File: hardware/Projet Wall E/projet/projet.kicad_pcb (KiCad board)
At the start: 2 copper layers, 91 parts, among them J201 USB_C_Receptacle_USB2.0_16P, J202 Conn_01x02, J301 Conn_ST_STDC14, J302 Conn_01x03, J401 Conn_01x06, J402 Conn_01x06, J501 Conn_01x06, J502 Conn_01x06, J503 Conn_01x03, J504 Conn_01x06, Q201 2SK3019, Q202 MMDT5401, Q203 DMP3099L, U201 AP2112K-3.3, U202 BQ27220YZFR, U203 USBLC6-2SC6, U204 BQ25896RTW, U301 STM32G431RBTx, U401 DRV8833PWP, U501 SN74AHCT1G125DBVR, Y301 16MHz

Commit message: PCB : contour 80x40, trous de fixation M2.5, sérigraphie
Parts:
- added C313: 1u, Capacitor_SMD:C_0402_1005Metric, F.Cu at (103.9, 87.5)
- added H301: MountingHole_Pad, MountingHole:MountingHole_2.2mm_M2_Pad_Via, F.Cu at (130.2, 116.8)
- added H302: MountingHole_Pad, MountingHole:MountingHole_2.2mm_M2_Pad_Via, F.Cu at (130.0, 123.5)
- added H303: MountingHole_Pad, MountingHole:MountingHole_2.2mm_M2_Pad_Via, F.Cu at (130.0, 129.4)
- added H304: MountingHole_Pad, MountingHole:MountingHole_2.2mm_M2_Pad_Via, F.Cu at (130.0, 135.4)
- C202: value 1µ -> 1u
- C301, C302, C303, C304: value 100nF -> 100n
- C305: value 4.7u -> 4u7
- C307, C312: value 1uF -> 1u
- moved C503 72.3 mm to (152.6, 106.0), turned to 90 degrees
- moved C509 70.7 mm to (153.0, 84.0)
- moved C502 70.3 mm to (150.6, 106.0), turned to 90 degrees
- moved C506 69.5 mm to (152.6, 103.1), turned to 90 degrees
- moved C505 67.4 mm to (150.6, 103.1), turned to 90 degrees
- moved C504 66.3 mm to (144.1, 76.5)
- moved C507 66.3 mm to (147.0, 76.5)
- moved C501 66.3 mm to (141.3, 76.5)
- moved C508 65.7 mm to (148.5, 84.0)
- moved R502 61.8 mm to (156.5, 95.5), turned to 90 degrees
- moved R501 59.6 mm to (154.5, 95.5), turned to 90 degrees
- moved J501 54.7 mm to (132.7, 105.1), turned to 90 degrees
- moved D501 49.1 mm to (134.0, 81.0), turned to 90 degrees
- moved J502 48.9 mm to (132.7, 100.5), turned to 90 degrees
- moved U501 42.9 mm to (136.1, 74.0)
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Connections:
- D501 pad 2: unconnected-(D501-DOUT-Pad2) -> Net-(D501-DOUT)
- J503 pad 2: /Capteur/NP_5V -> Net-(D501-DOUT)

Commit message: Ajout points de test + plans de masse PCB
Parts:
- added TP201: GND, TestPoint:TestPoint_Pad_D1.5mm, F.Cu at (104.1, 66.4)
- added TP202: VSYS, TestPoint:TestPoint_Pad_D1.0mm, F.Cu at (107.4, 66.1)
- added TP203: +3.3V, TestPoint:TestPoint_Pad_D1.0mm, F.Cu at (107.4, 69.2)
- added TP204: +5V_USB, TestPoint:TestPoint_Pad_D1.0mm, F.Cu at (110.4, 66.1)
- added TP205: VBUS, TestPoint:TestPoint_Pad_D1.0mm, F.Cu at (110.4, 69.2)
- added TP206: BAT, TestPoint:TestPoint_Pad_D1.0mm, F.Cu at (113.5, 66.1)
- added TP207: SCL, TestPoint:TestPoint_Pad_D1.0mm, F.Cu at (113.5, 69.2)
- added TP208: SDA, TestPoint:TestPoint_Pad_D1.0mm, F.Cu at (116.5, 66.1)
- added TP209: CHG_INT, TestPoint:TestPoint_Pad_D1.0mm, F.Cu at (116.5, 69.2)
- added TP210: GND, TestPoint:TestPoint_Pad_D1.5mm, F.Cu at (104.1, 69.9)
- added TP211: GND, TestPoint:TestPoint_Pad_D1.5mm, F.Cu at (104.1, 73.5)
- added TP401: MOT_nFAULT, TestPoint:TestPoint_Pad_D1.0mm, F.Cu at (108.9, 78.8)
- added TP501: SCL_CAPT, TestPoint:TestPoint_Pad_D1.0mm, F.Cu at (103.8, 78.8)
- added TP502: SDA_CAPT, TestPoint:TestPoint_Pad_D1.0mm, F.Cu at (103.8, 81.8)
- C201, C202, C203, C204, C205, C206, C207, C208, C209, C210, C211, C212, C401, C402, C403, D201, D202, F201, L201, Q201, Q202, Q203, R201, R202, R203, R204, R205, R206, R207, R208, R209, R210, R211, R212, R213, R214, R215, R216, R217, R218, R401, R402, R403, U201, U202, U203, U204, U401: moved to B.Cu
- moved R211 136.2 mm to (197.7, 82.3), turned to 180 degrees
- moved J201 135.9 mm to (200.2, 68.6), turned to 90 degrees
- moved R208 134.6 mm to (196.0, 76.8)
- moved R202 131.6 mm to (191.4, 63.9), turned to 180 degrees
- moved R203 131.6 mm to (191.4, 65.1), turned to 180 degrees
- moved R205 130.8 mm to (189.8, 78.9), turned to -90 degrees
- moved R207 130.2 mm to (190.9, 78.9), turned to 90 degrees
- moved Q203 127.6 mm to (200.2, 78.8), turned to 90 degrees
- moved J302 121.9 mm to (187.5, 87.0), turned to 90 degrees
- moved R206 119.6 mm to (178.0, 84.5), turned to 180 degrees
- moved Q202 119.1 mm to (196.4, 78.8)
- moved J202 118.9 mm to (191.2, 55.5), turned to 180 degrees
- moved C201 118.2 mm to (174.4, 63.6), turned to 135 degrees
- moved U203 118.1 mm to (190.8, 68.5), turned to 90 degrees
- moved R303 118.0 mm to (186.0, 81.2)
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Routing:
- net GND: track 0.00 -> 23.8 mm, vias 0 -> 73
- added copper zone on In1.Cu, net GND
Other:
- copper layers 2 -> 4

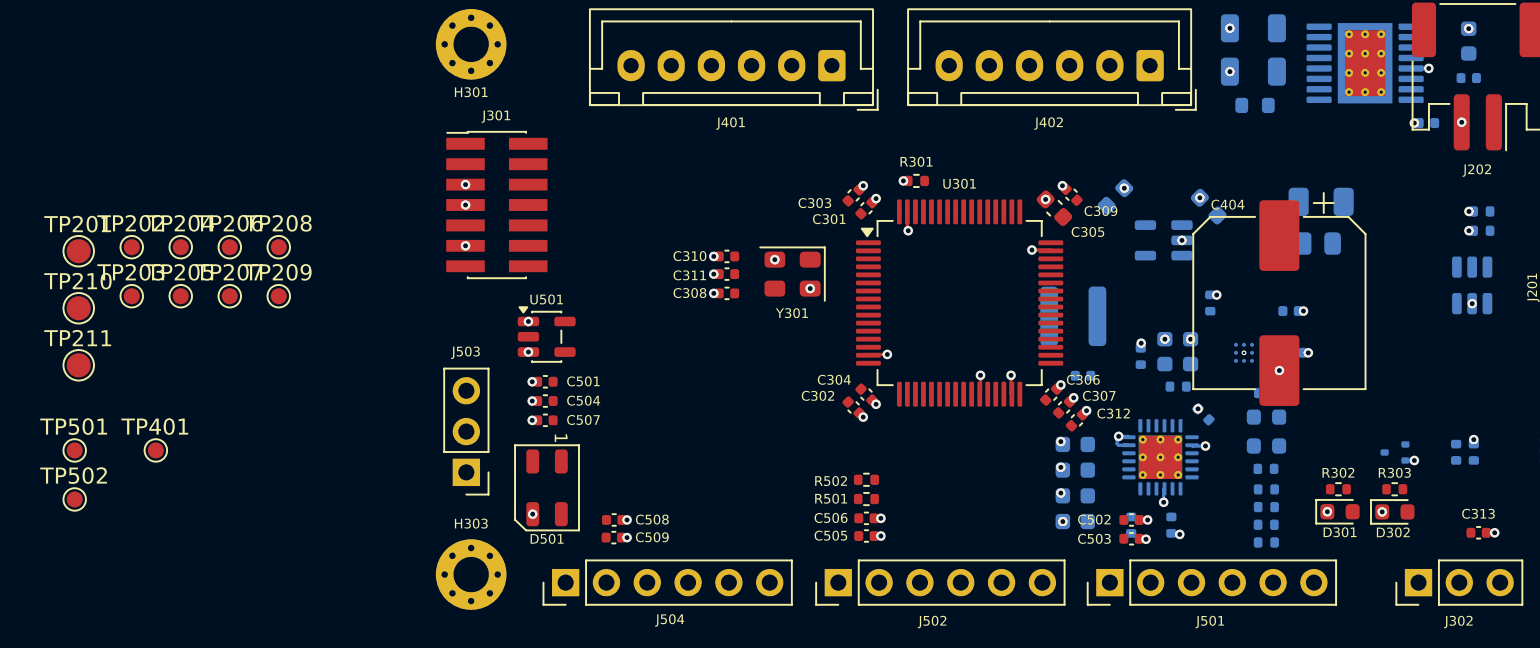
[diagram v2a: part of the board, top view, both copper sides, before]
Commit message: PCB : placement composants et points de test
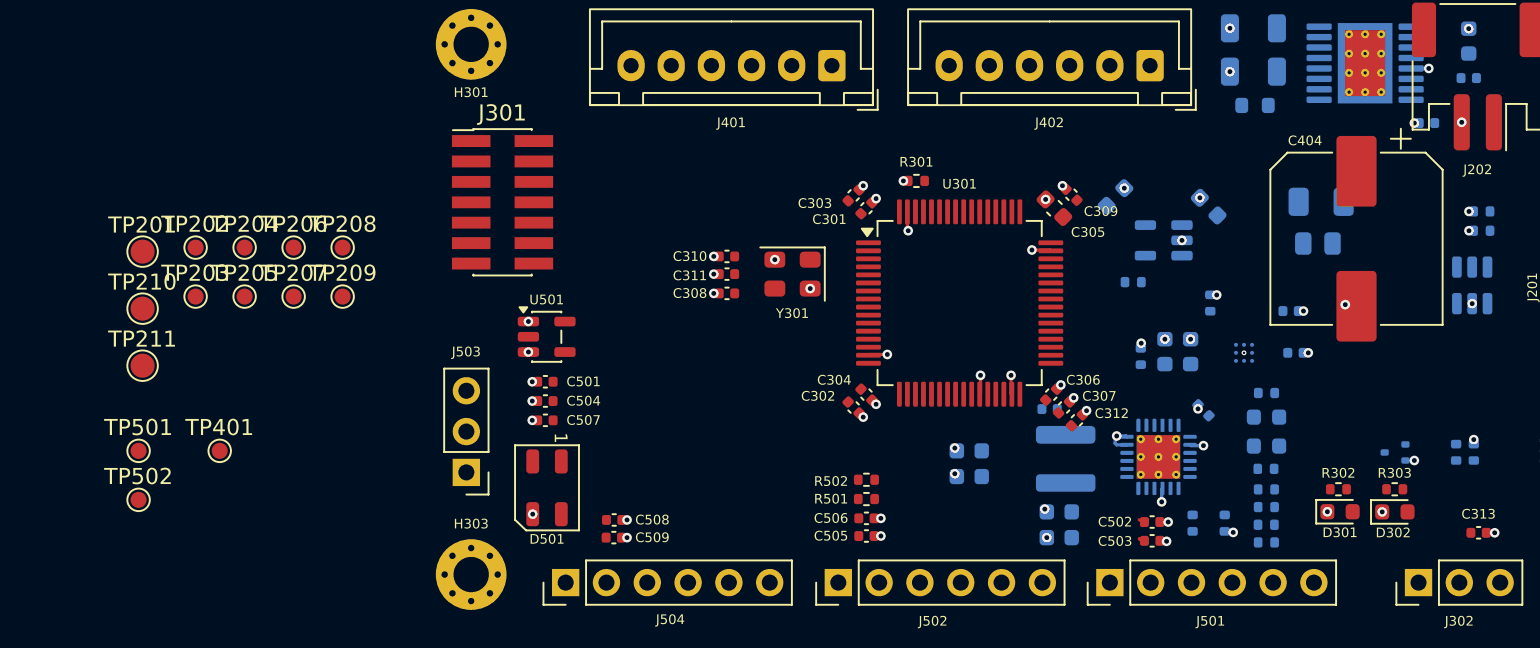
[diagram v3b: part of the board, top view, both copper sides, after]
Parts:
- moved L201 8.89 mm to (165.5, 79.3), turned to -90 degrees
- moved R204 7.08 mm to (169.7, 68.3)
- moved C210 6.61 mm to (159.5, 80.4)
- moved C211 6.61 mm to (159.5, 78.8)
- moved C404 6.25 mm to (183.6, 65.6)
- moved TP204 3.98 mm to (114.4, 66.2)
- moved TP205 3.98 mm to (114.4, 69.2)
- moved TP206 3.98 mm to (117.5, 66.2)
- moved TP207 3.98 mm to (117.5, 69.2)
- moved TP201 3.98 mm to (108.0, 66.4)
- moved TP202 3.98 mm to (111.3, 66.2)
- moved TP203 3.98 mm to (111.3, 69.2)
- moved TP208 3.98 mm to (120.5, 66.2)
- moved TP209 3.98 mm to (120.5, 69.2)
- moved TP210 3.98 mm to (108.0, 70.0)
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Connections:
- C501 pad 1: VBUS -> +5V_USB
- C504 pad 2: VBUS -> +5V_USB
- D501 pad 1: VBUS -> +5V_USB
- R216 pad 1: Net-(U204-REGN) -> Net-(U204-TS)
- R216 pad 2: Net-(U204-TS) -> Net-(U204-REGN)
- R217 pad 1: Net-(U204-REGN) -> Net-(U204-TS)
- U501 pad 5: VBUS -> +5V_USB
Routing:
- net GND: track 23.8 -> 22.9 mm, vias 73 -> 70
- net +3.3V: track 0.00 -> 0.95 mm

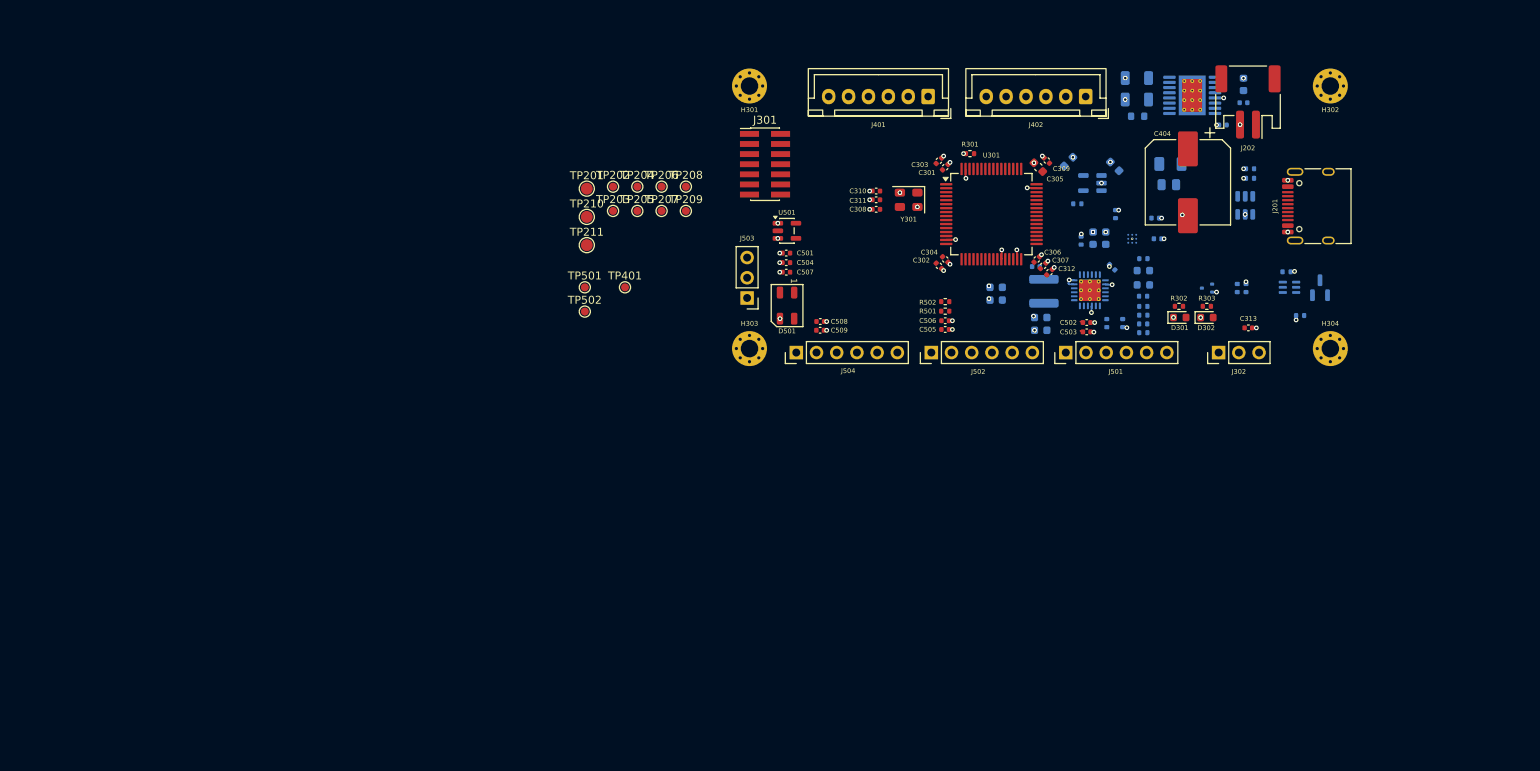
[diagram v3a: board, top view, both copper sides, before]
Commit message: correction erreur drc
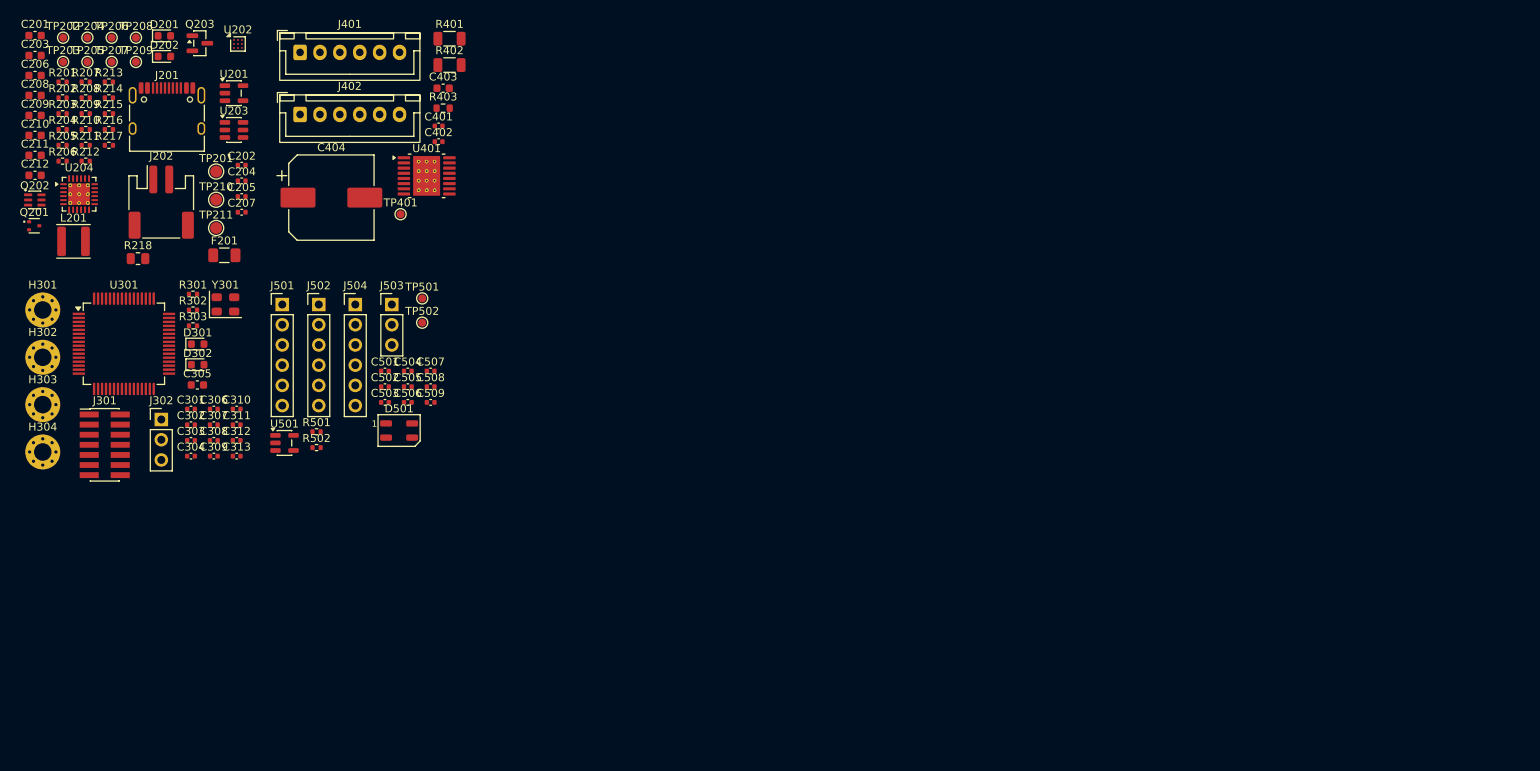
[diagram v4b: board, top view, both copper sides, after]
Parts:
- C201, C202, C203, C204, C205, C206, C207, C208, C209, C210, C211, C212, C401, C402, C403, D201, D202, F201, L201, Q201, Q202, Q203, R201, R202, R203, R204, R205, R206, R207, R208, R209, R210, R211, R212, R213, R214, R215, R216, R217, R218, R401, R402, R403, U201, U202, U203, U204, U401: moved to F.Cu
- moved H302 165.4 mm to (39.7, 87.6)
- moved H304 162.3 mm to (39.7, 99.5)
- moved Q202 158.1 mm to (38.7, 67.8)
- moved R211 154.1 mm to (45.1, 61.0), turned to 0 degrees
- moved R208 152.5 mm to (45.1, 55.0)
- moved R202 149.5 mm to (42.2, 55.0), turned to 0 degrees
- moved R203 149.5 mm to (42.2, 57.0), turned to 0 degrees
- moved R205 148.7 mm to (42.2, 61.0), turned to 0 degrees
- moved R207 148.1 mm to (45.1, 53.0), turned to 0 degrees
- moved Q201 147.6 mm to (38.6, 71.1), turned to 0 degrees
- moved J201 145.3 mm to (55.3, 57.8), turned to 0 degrees
- moved Q203 144.1 mm to (59.4, 48.1), turned to 0 degrees
- moved R206 137.5 mm to (42.2, 62.9), turned to 0 degrees
- moved J202 137.2 mm to (54.6, 68.1), turned to 0 degrees
- moved C201 136.7 mm to (38.7, 47.2), turned to 0 degrees
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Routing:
- net GND: track 22.9 -> 0.00 mm, vias 70 -> 0
- net +3.3V: track 0.95 -> 0.00 mm
- removed copper zone on In1.Cu, net GND

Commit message: (feat : Placement PCB 10*6cm et mise à jour TestPoint)
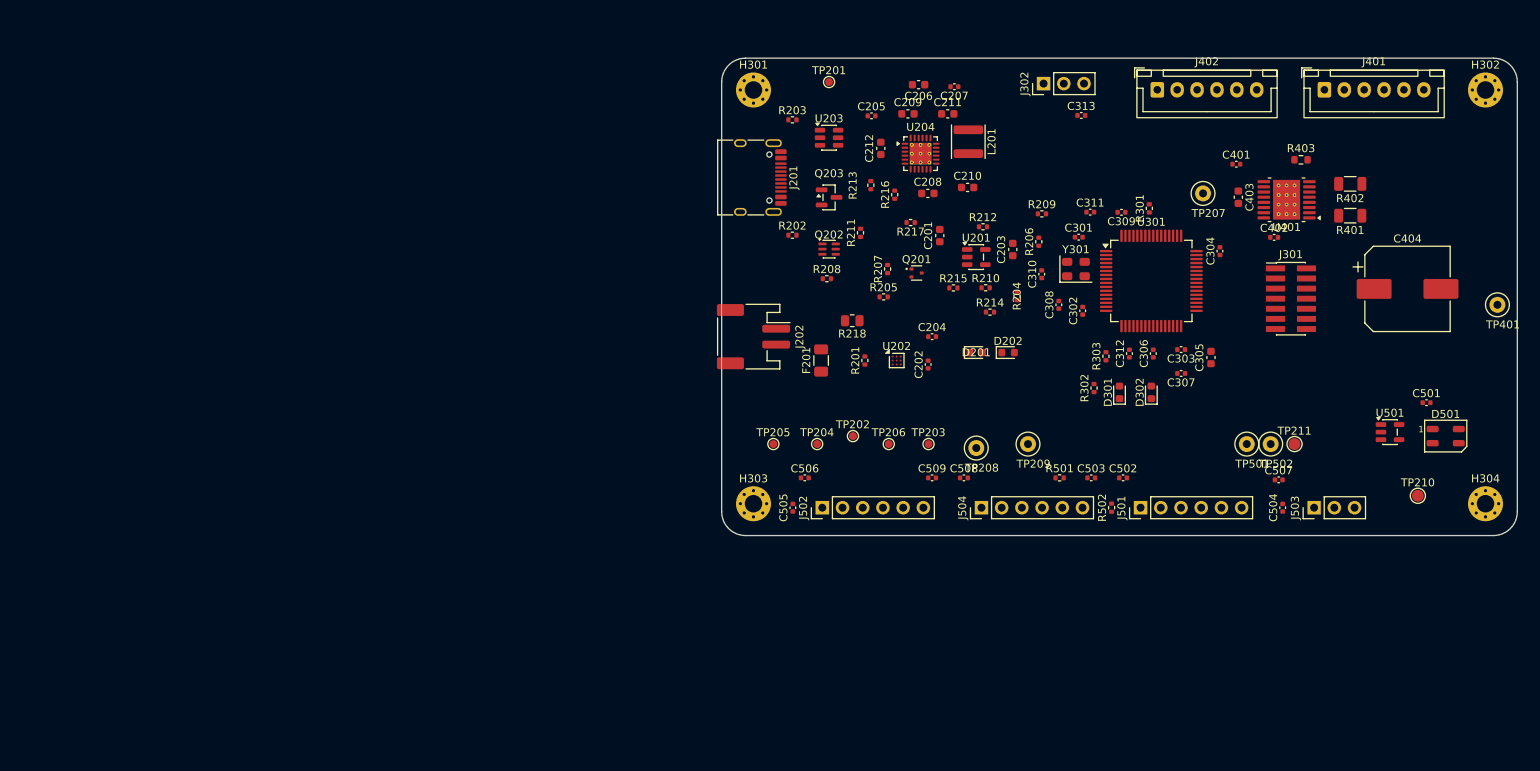
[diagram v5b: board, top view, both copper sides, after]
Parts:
- TP201: footprint TestPoint:TestPoint_Pad_D1.5mm -> TestPoint:TestPoint_Pad_D1.0mm
- TP207, TP208, TP209, TP401, TP501, TP502: footprint TestPoint:TestPoint_Pad_D1.0mm -> TestPoint:TestPoint_Loop_D2.50mm_Drill1.0mm
- moved H302 184.4 mm to (221.0, 54.0)
- moved H304 181.4 mm to (221.0, 106.0)
- moved TP210 155.5 mm to (212.5, 105.0)
- moved J301 150.2 mm to (196.6, 80.2)
- moved U501 139.0 mm to (209.0, 97.0)
- moved TP401 138.3 mm to (222.5, 81.0)
- moved TP211 138.2 mm to (197.0, 98.5)
- moved TP207 138.2 mm to (185.5, 67.0)
- moved C404 135.7 mm to (211.2, 79.0)
- moved C304 131.9 mm to (187.6, 74.2), turned to 90 degrees
- moved D501 131.5 mm to (216.0, 97.5)
- moved C501 131.0 mm to (213.6, 93.3)
- moved U301 129.4 mm to (179.0, 78.0)
- moved J401 128.8 mm to (200.8, 54.0)
- moved C305 127.4 mm to (186.5, 87.6), turned to 90 degrees
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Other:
- board outline added: 100 x 60 mm
